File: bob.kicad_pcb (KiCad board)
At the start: 4 copper layers, 58.4 x 25.4 mm, 64 parts, among them J1 Micro USB Female, J2 Screw Terminal, 2.54mm, J3 GPIO (Optional), J4 GPIO (Optional), J5 Conn_01x03_Male, J6 Conn_01x06_Pin, Q1 AO3400A, Q2 AO3400A, Q3 AO3400A, SW1 Bootsel, U1 AMS1117-3.3, U2 W25Q128JVSS, U3 QMC5883L, U4 HP203B, U5 RP2040, U6 QMI8658C, U7 W25Q128JVSS, Y1 12MHz

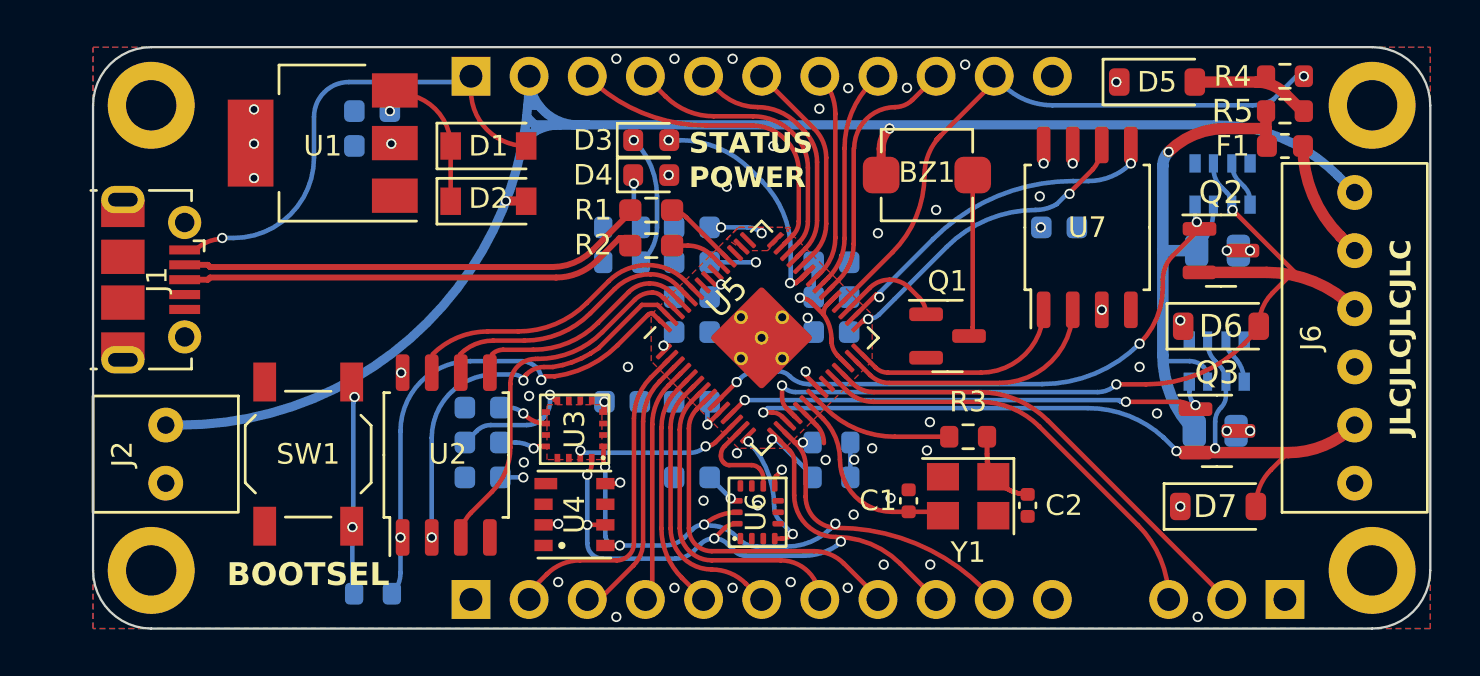
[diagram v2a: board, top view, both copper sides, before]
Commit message: Reroute PCB to match changes in schematic
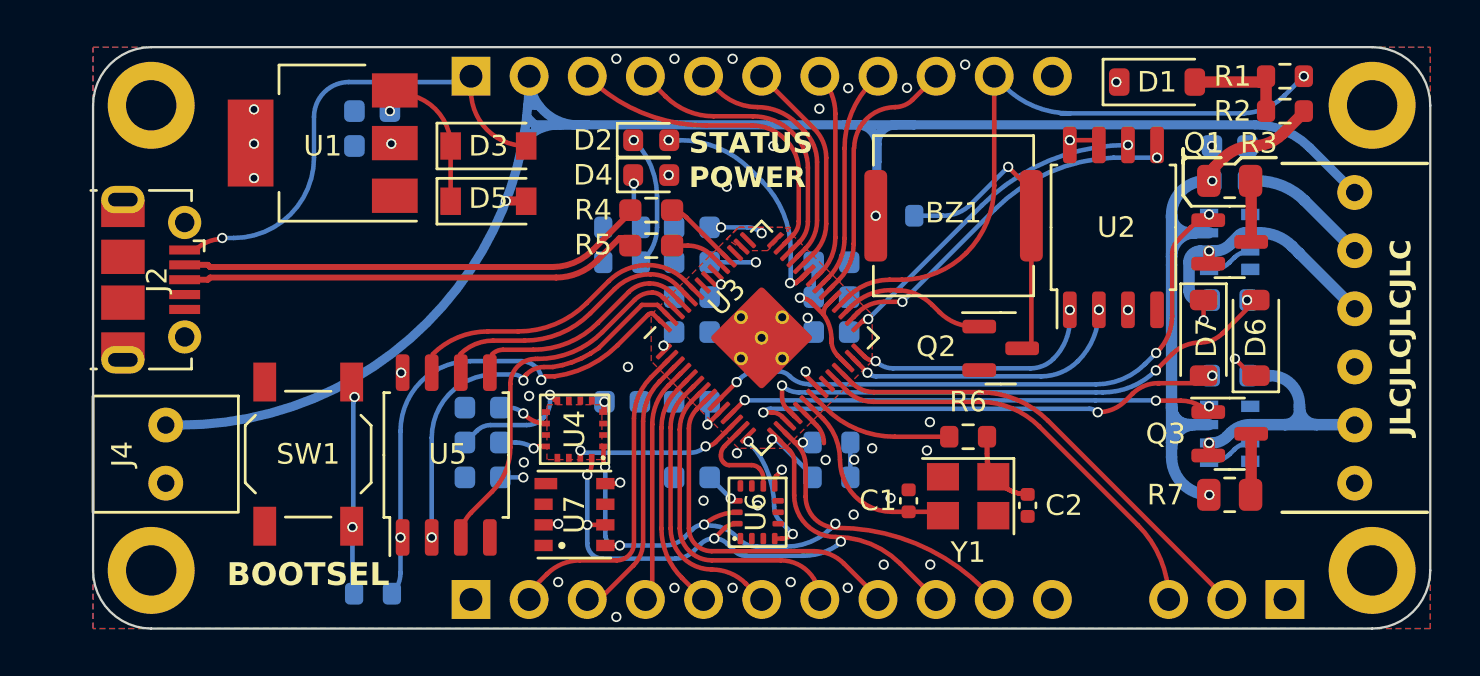
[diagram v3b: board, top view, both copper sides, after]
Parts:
- removed the C3 at (56.2, 25.7)
- removed the R6 at (63.1, 26.7)
- removed the U7 at (57.4, 25.7)
- added C5: 100n, Capacitor_SMD:C_0603_1608Metric, B.Cu at (63.6, 22.1)
- added R11: 10k, Resistor_SMD:R_0603_1608Metric, B.Cu at (63.6, 28.8)
- added R12: 10k, Resistor_SMD:R_0603_1608Metric, B.Cu at (63.6, 32.1)
- added R3: 5, Resistor_SMD:R_0805_2012Metric, F.Cu at (63.6, 23.6)
- added R8: 1k, Resistor_SMD:R_0603_1608Metric, B.Cu at (49.0, 25.1)
- added U2: W25Q128JVSS, Package_SO:SOIC-8_5.23x5.23mm_P1.27mm, F.Cu at (58.5, 25.7)
- BZ1: footprint YAR_other:Cy-SMD-4020-3040 -> YAR_other:CPT-7502-65-SMT-TR
- F1: moved to B.Cu
- R7: value 4 -> 5; moved to F.Cu
- R9: renamed from R10; value 220 -> 470
- moved Q1 13.0 mm to (63.6, 26.3)
- moved Q2 10.5 mm to (53.6, 30.9)
- moved D7 7.39 mm to (62.5, 30.5), turned to -90 degrees
- moved RN2 3.22 mm to (63.6, 34.7), turned to 180 degrees
- moved R7 2.87 mm to (63.6, 37.3)
- moved F1 2.85 mm to (63.6, 23.6)
- moved RN1 2.55 mm to (63.6, 26.3), turned to 180 degrees
- moved BZ1 2.12 mm to (51.6, 25.1)
- moved D6 1.61 mm to (64.8, 30.5), turned to 90 degrees
- moved Q3 0.57 mm to (63.6, 34.7)
- turned R2 to 0 degrees
- renumbered C5 to C10, C10 to C11, C6 to C12, C14 to C13, C13 to C14, C11 to C15, C15 to C16, C16 to C17, C12 to C18, C17 to C3, C18 to C4, C7 to C6, C8 to C7, C4 to C8, D5 to D1, D3 to D2, D1 to D3, D2 to D5, H3 to H1, H1 to H2, H4 to H3, H2 to H4, J3 to J1, J1 to J2, J6 to J3, J2 to J4, J4 to J6, R4 to R1, R11 to R10, R8 to R13, R9 to R14, R12 to R15, R5 to R2, R1 to R4, R2 to R5, R3 to R6, U5 to U3, U3 to U4, U2 to U5, U4 to U7
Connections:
- J3 pad 2: Cont 2 -> /Pyro 2/Fire +
- J3 pad 4: Cont 1 -> /Pyro 1/Fire +
- Q1 pad 1: BUZZER -> Pyro 1
- Q1 pad 2: GND -> /Pyro 1/Fire +
- Q1 pad 3: Net-(BZ1-+) -> Net-(Q2-D)
- Q2 pad 1: Pyro 1 -> BUZZER
- Q2 pad 2: Cont 1 -> GND
- Q2 pad 3: Net-(Q2-D) -> Net-(BZ1-+)
- Q3 pad 2: Cont 2 -> /Pyro 2/Fire +
- RN1 pad 2: Cont 1 -> /Pyro 1/Fire +
- RN1 pad 6: Cont 1 -> /Pyro 1/Fire +
- RN2 pad 2: Cont 2 -> /Pyro 2/Fire +
- RN2 pad 6: Cont 2 -> /Pyro 2/Fire +
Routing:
- net Cont 1: track 39.2 -> 24.3 mm
- net Cont 2: track 35.9 -> 21.3 mm
- net /Pyro 2/Fire +: track 0.00 -> 12.5 mm, vias 0 -> 1
- net /Pyro 1/Fire +: track 0.00 -> 12.3 mm, vias 0 -> 1
- net ARM: track 24.3 -> 31.3 mm, vias 1 -> 2
- net Net-(BZ1-+): track 7.07 -> 13.6 mm, vias 0 -> 1
- net +BATT: track 70.9 -> 76.8 mm
- net +3V3: track 18.9 -> 22.4 mm, vias 27 -> 26
- net ARMED: track 26.2 -> 29.4 mm
- net Net-(Q3-D): track 0.00 -> 2.67 mm, vias 2 -> 0
- net Net-(Q2-D): track 0.00 -> 2.67 mm, vias 2 -> 0
- net BUZZER: track 4.60 -> 6.73 mm
- net SPI_CS: track 9.69 -> 11.1 mm, vias 0 -> 2
- net SPI_RX: track 11.5 -> 12.9 mm, vias 0 -> 2
- net SPI_TX: track 14.5 -> 15.8 mm
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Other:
- board text added: "Bob Rev 4B Claire H 2025"
- board text removed: "Bob Rev 4A Claire H 2023"
